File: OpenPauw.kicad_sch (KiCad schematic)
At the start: 5 parts, among them U1 MAX328EPE+, U2 MAX328EPE+, U3 MAX328EPE+, U4 MAX328EPE+, U5 Adafruit-Feather-RP2040

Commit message: added
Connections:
- net 3.3 V Rail: no longer U1.13 (V+), U2.13 (V+), U3.13 (V+), U4.13 (V+)
- net GND: now also U1.3 (V-), U2.3 (V-), U3.3 (V-), U4.3 (V-)
- net I_MINUS: now also U2.8 (D)
- net I_PLUS: now also U1.8 (D)
- net PAD_A: now also U1.4 (S1), U2.4 (S1), U3.4 (S1), U4.4 (S1)
- net PAD_B: now also U1.5 (S2), U2.5 (S2), U3.5 (S2), U4.5 (S2)
- net PAD_C: now also U1.6 (S3), U2.6 (S3), U3.6 (S3), U4.6 (S3)
- net PAD_D: now also U1.7 (S4), U2.7 (S4), U3.7 (S4), U4.7 (S4)
- net V_MINUS: now also U4.8 (D)
- net V_PLUS: now also U3.8 (D)

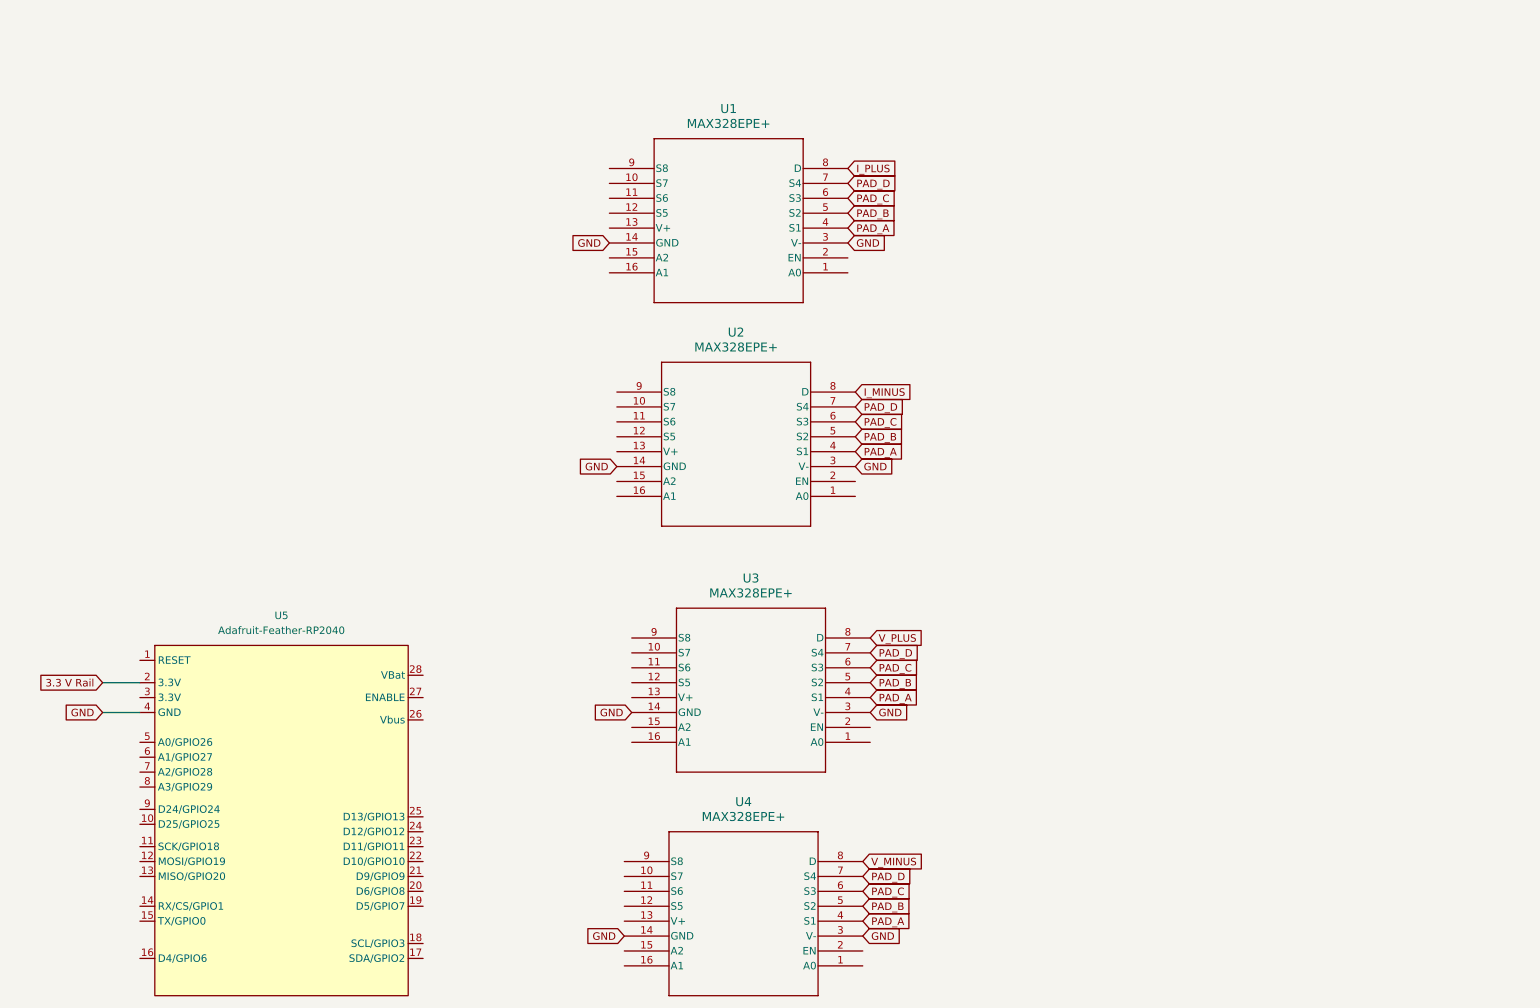
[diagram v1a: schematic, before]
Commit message: adding 15v boost circuit
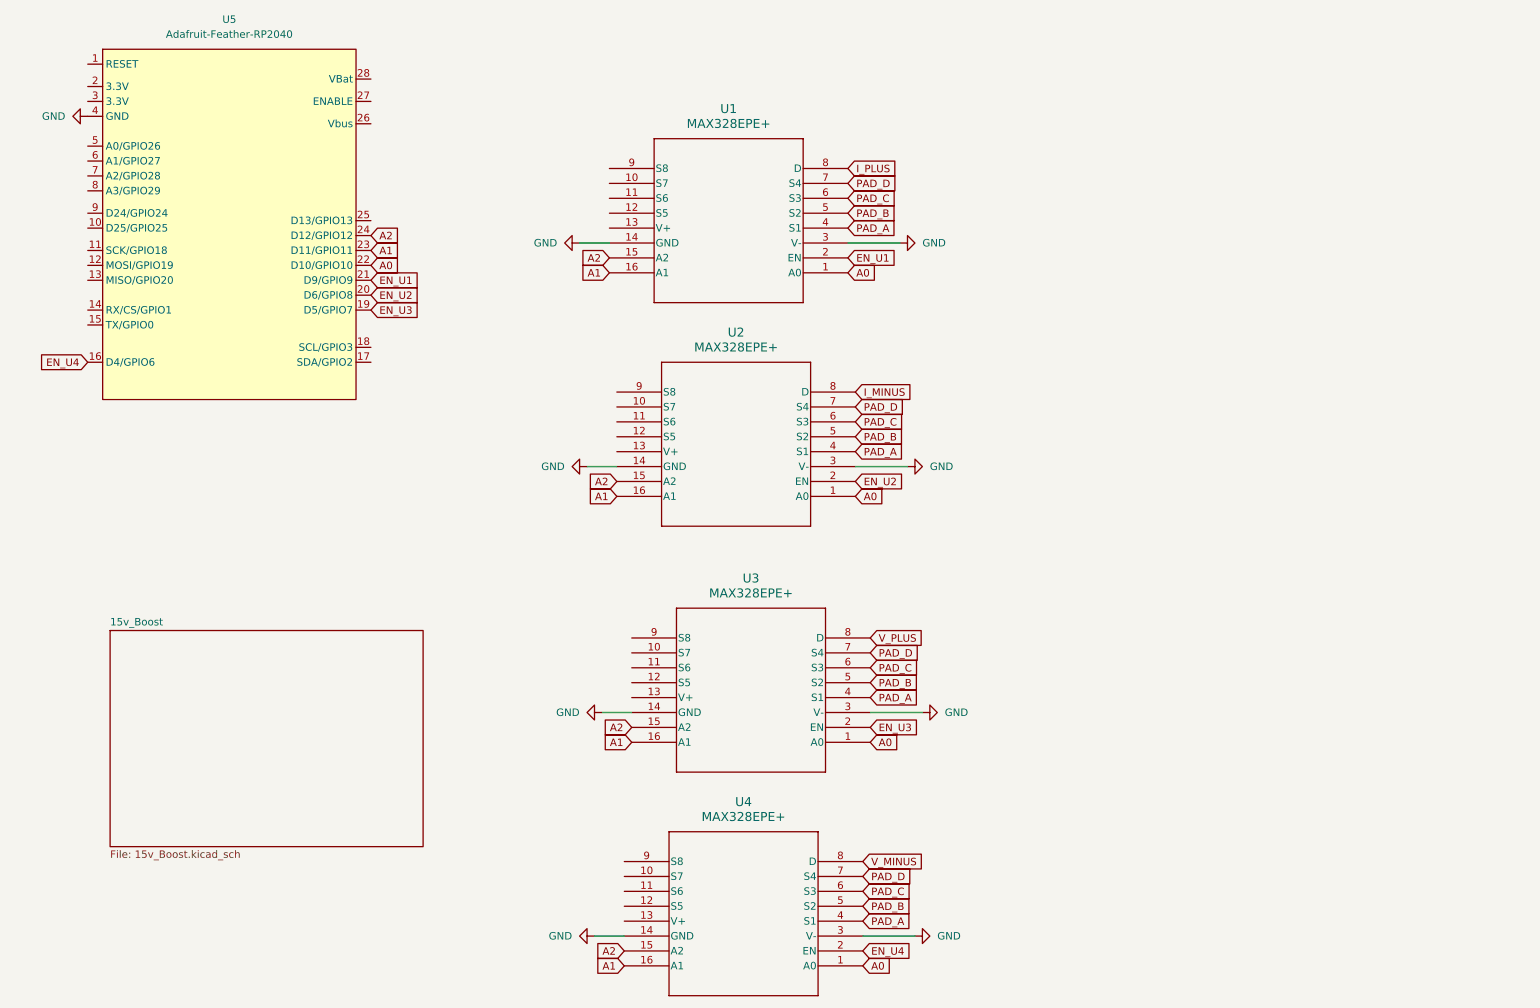
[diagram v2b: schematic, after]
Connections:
- net A0: now reaches U4.1 (A0)
- net A0: now also U1.1 (A0), U2.1 (A0), U3.1 (A0), U5.22 (D10/GPIO10)
- net A2: now reaches U4.15 (A2)
- net A2: now also U1.15 (A2), U2.15 (A2), U3.15 (A2), U5.24 (D12/GPIO12)
- net A1: now reaches U4.16 (A1)
- net A1: now also U1.16 (A1), U2.16 (A1), U3.16 (A1), U5.23 (D11/GPIO11)
- net EN_U4: now reaches U4.2 (EN)
- net EN_U4: now also U5.16 (D4/GPIO6)
- net EN_U1: now reaches U1.2 (EN)
- net EN_U1: now also U5.21 (D9/GPIO9)
- net EN_U3: now reaches U3.2 (EN)
- net EN_U3: now also U5.19 (D5/GPIO7)
- net EN_U2: now reaches U2.2 (EN)
- net EN_U2: now also U5.20 (D6/GPIO8)
- net 3.3 V Rail: no longer names the net of U5.2 (3.3V)
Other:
- added sheet 15v_Boost (15v_Boost.kicad_sch)
- moved on the sheet: U5

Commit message: finalized schematic ready for layout
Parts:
- added J1, J2, J3, J4: Conn_01x01, Connector:Banana_Cliff_FCR7350B_S16N-PC_Horizontal, symbol Connector_Generic:Conn_01x01
- added J5: Conn_01x04, Connector_JST:JST_GH_BM04B-GHS-TBT_1x04-1MP_P1.25mm_Vertical, symbol Connector_Generic:Conn_01x04
- U1, U2, U3, U4: footprint 221-0043_P16+2_MXM -> Package_DIP:DIP-16_W7.62mm_Socket_LongPads; URL (none) -> https://www.digikey.com/en/products/detail/analog-devices-i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
- U5: footprint (none) -> Library:Adafruit-Feather-RP2040
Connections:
- net I_MINUS: now also J2.1 (Pin_1)
- net I_PLUS: now also J1.1 (Pin_1)
- net PAD_A: now also J5.1 (Pin_1)
- net PAD_B: now also J5.2 (Pin_2)
- net PAD_C: now also J5.3 (Pin_3)
- net PAD_D: now also J5.4 (Pin_4)
- net V_MINUS: now also J4.1 (Pin_1)
- net V_PLUS: now also J3.1 (Pin_1)
- net +15V: now reaches U4.13 (V+)
- net +15V: now also U1.13 (V+), U2.13 (V+), U3.13 (V+)
- net +5V: now reaches U5.26 (Vbus)
- no-connect marks 0 -> 35

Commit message: New layout
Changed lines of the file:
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@@
 					(size 1.27 1.27)
 				)
-				(hide yes)
 			)
 		)

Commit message: New JST
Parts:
- J5: footprint Connector_JST:JST_GH_BM04B-GHS-TBT_1x04-1MP_P1.25mm_Vertical -> Connector_JST:JST_PH_B4B-PH-SM4-TB_1x04-1MP_P2.00mm_Vertical
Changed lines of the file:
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@@
 			)
 		)
-		(property "Footprint" "Connector_JST:JST_GH_BM04B-GHS-TBT_1x04-1MP_P1.25mm_Vertical"
+		(property "Footprint" "Connector_JST:JST_PH_B4B-PH-SM4-TB_1x04-1MP_P2.00mm_Vertical"
 			(at 256.54 63.5 0)
 			(effects
